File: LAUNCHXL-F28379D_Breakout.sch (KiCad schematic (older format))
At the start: 30 parts, among them Q1 100V/17A, Q2 100V/17A, Q3 100V/17A, Q4 100V/17A, Q5 100V/17A, Q6 100V/17A, U2 TL084CN, U5 STK681-332-E

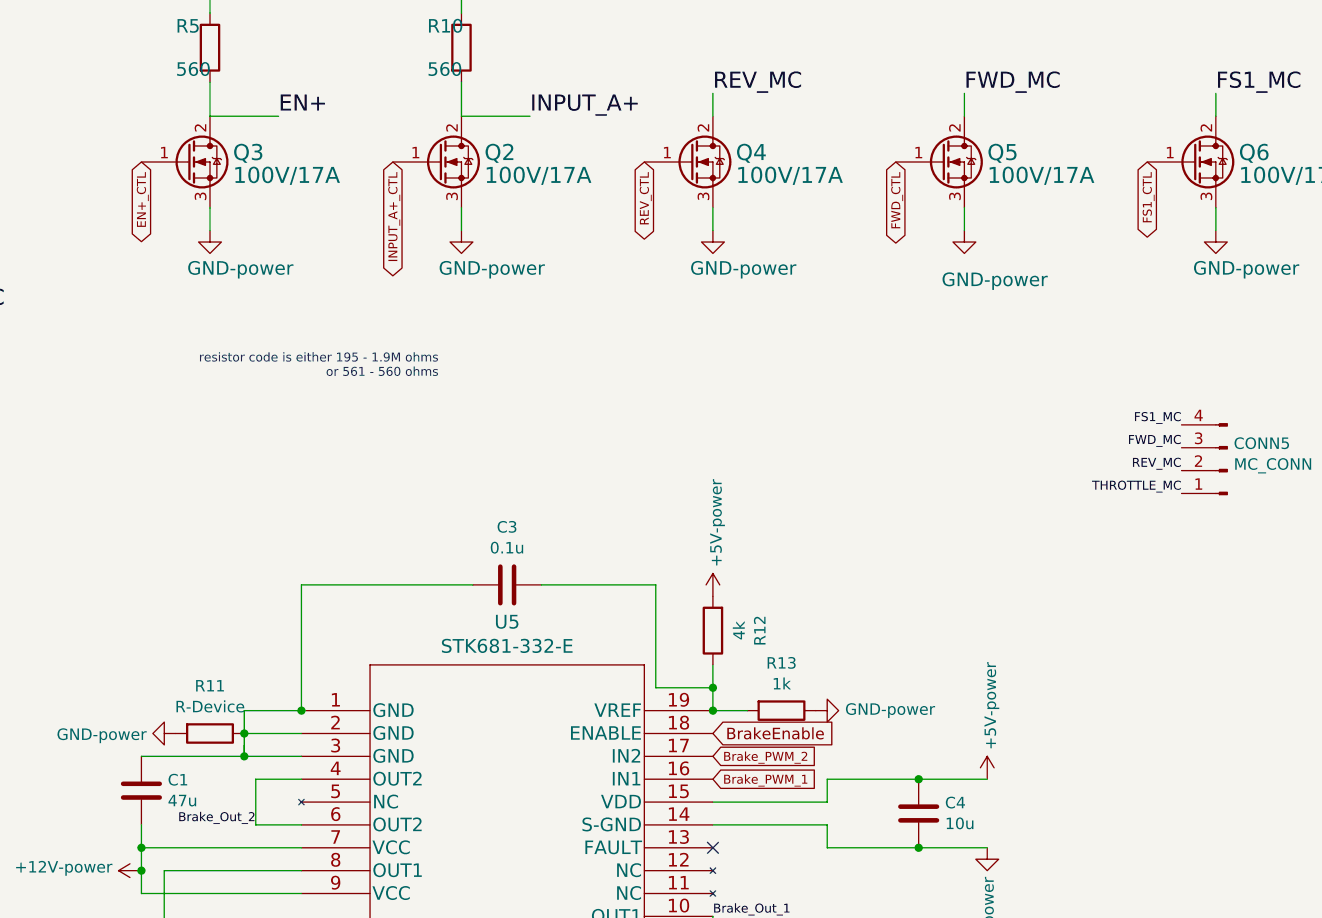
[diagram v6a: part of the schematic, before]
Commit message: updated PCB with bluetooth connector for arduino signals
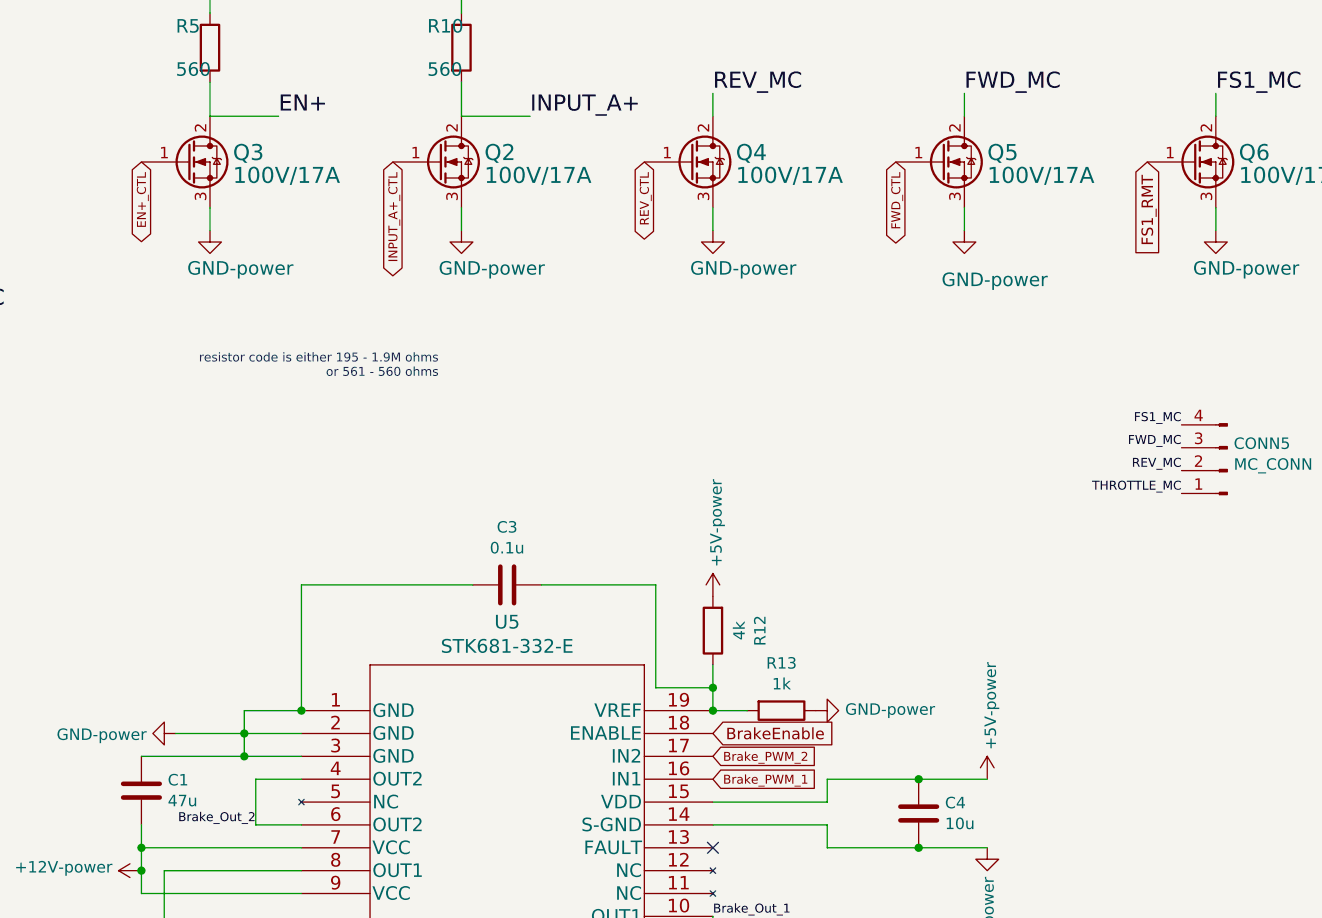
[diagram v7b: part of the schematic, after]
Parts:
- removed R11: R-Device, Resistor_THT:R_Axial_DIN0204_L3.6mm_D1.6mm_P1.90mm_Vertical, symbol PCB_2020-rescue:R-Device
- C1: footprint Capacitor_THT:C_Disc_D3.0mm_W1.6mm_P2.50mm -> Capacitor_THT:C_Radial_D4.0mm_H5.0mm_P1.50mm
- C3, C4: footprint Capacitor_THT:C_Disc_D3.0mm_W1.6mm_P2.50mm -> Capacitor_THT:CP_Radial_D4.0mm_P1.50mm
- R1, R12, R13, R18, R2, R3, R4, R5, R6, R7, R8, R9: footprint Resistor_THT:R_Axial_DIN0204_L3.6mm_D1.6mm_P1.90mm_Vertical -> Resistor_THT:R_Axial_DIN0204_L3.6mm_D1.6mm_P7.62mm_Horizontal
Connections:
- net GND: now also C1.2, C3.1, U5.1 (GND), U5.2 (GND), U5.3 (GND)
- net FS1_CTL renamed FS1_RMT
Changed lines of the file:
@@
 Text GLabel 9700 3200 3    39   BiDi ~ 0
 FWD_CTL
-Text GLabel 10800 3200 3    39   BiDi ~ 0
-FS1_CTL
 Text GLabel 7500 3200 3    39   BiDi ~ 0
 INPUT_A+_CTL
@@
 F 0 "R1" H 4600 1550 59  0000 L BNN
 F 1 "10k" H 4550 1450 59  0000 L BNN
-F 2 "Resistor_THT:R_Axial_DIN0204_L3.6mm_D1.6mm_P1.90mm_Vertical" H 4800 1500 50  0001 C CNN
+F 2 "Resistor_THT:R_Axial_DIN0204_L3.6mm_D1.6mm_P7.62mm_Horizontal" H 4800 1500 50  0001 C CNN
 F 3 "" H 4800 1500 50  0001 C CNN
 	1    4800 1500
@@
 F 0 "R5" H 6550 2759 59  0000 L BNN
 F 1 "560" H 6550 2570 59  0000 L BNN
-F 2 "Resistor_THT:R_Axial_DIN0204_L3.6mm_D1.6mm_P1.90mm_Vertical" H 6700 2700 50  0001 C CNN
+F 2 "Resistor_THT:R_Axial_DIN0204_L3.6mm_D1.6mm_P7.62mm_Horizontal" H 6700 2700 50  0001 C CNN
 F 3 "" H 6700 2700 50  0001 C CNN
 	1    6700 2700
@@
 F 0 "R10" H 7650 2759 59  0000 L BNN
 F 1 "560" H 7650 2570 59  0000 L BNN
-F 2 "Resistor_THT:R_Axial_DIN0204_L3.6mm_D1.6mm_P1.90mm_Vertical" H 7800 2700 50  0001 C CNN
+F 2 "Resistor_THT:R_Axial_DIN0204_L3.6mm_D1.6mm_P7.62mm_Horizontal" H 7800 2700 50  0001 C CNN
 F 3 "" H 7800 2700 50  0001 C CNN
 	1    7800 2700
@@
 F 0 "R2" H 5600 1500 59  0000 L BNN
 F 1 "10k" H 5550 1400 59  0000 L BNN
-F 2 "Resistor_THT:R_Axial_DIN0204_L3.6mm_D1.6mm_P1.90mm_Vertical" H 5800 1500 50  0001 C CNN
+F 2 "Resistor_THT:R_Axial_DIN0204_L3.6mm_D1.6mm_P7.62mm_Horizontal" H 5800 1500 50  0001 C CNN
 F 3 "" H 5800 1500 50  0001 C CNN
 	1    5800 1500
@@
 F 0 "R3" V 3143 3950 50  0000 C CNN
 F 1 "1000" V 3234 3950 50  0000 C CNN
-F 2 "Resistor_THT:R_Axial_DIN0204_L3.6mm_D1.6mm_P1.90mm_Vertical" V 3280 3950 50  0001 C CNN
+F 2 "Resistor_THT:R_Axial_DIN0204_L3.6mm_D1.6mm_P7.62mm_Horizontal" V 3280 3950 50  0001 C CNN
 F 3 "" H 3350 3950 50  0001 C CNN
 	1    3350 3950
@@
 F 0 "R7" V 4093 4750 50  0000 C CNN
 F 1 "5400" V 4184 4750 50  0000 C CNN
-F 2 "Resistor_THT:R_Axial_DIN0204_L3.6mm_D1.6mm_P1.90mm_Vertical" V 4230 4750 50  0001 C CNN
+F 2 "Resistor_THT:R_Axial_DIN0204_L3.6mm_D1.6mm_P7.62mm_Horizontal" V 4230 4750 50  0001 C CNN
 F 3 "" H 4300 4750 50  0001 C CNN
 	1    4300 4750
@@
 F 0 "R6" H 3420 3096 50  0000 L CNN
 F 1 "5400" H 3420 3005 50  0000 L CNN
-F 2 "Resistor_THT:R_Axial_DIN0204_L3.6mm_D1.6mm_P1.90mm_Vertical" V 3280 3050 50  0001 C CNN
+F 2 "Resistor_THT:R_Axial_DIN0204_L3.6mm_D1.6mm_P7.62mm_Horizontal" V 3280 3050 50  0001 C CNN
 F 3 "" H 3350 3050 50  0001 C CNN
 	1    3350 3050
@@
 F 0 "R4" V 2893 3400 50  0000 C CNN
 F 1 "1000" V 2984 3400 50  0000 C CNN
-F 2 "Resistor_THT:R_Axial_DIN0204_L3.6mm_D1.6mm_P1.90mm_Vertical" V 3030 3400 50  0001 C CNN
+F 2 "Resistor_THT:R_Axial_DIN0204_L3.6mm_D1.6mm_P7.62mm_Horizontal" V 3030 3400 50  0001 C CNN
 F 3 "" H 3100 3400 50  0001 C CNN
 	1    3100 3400
@@
 F 0 "R9" V 2743 4100 50  0000 C CNN
 F 1 "1000" V 2834 4100 50  0000 C CNN
-F 2 "Resistor_THT:R_Axial_DIN0204_L3.6mm_D1.6mm_P1.90mm_Vertical" V 2880 4100 50  0001 C CNN
+F 2 "Resistor_THT:R_Axial_DIN0204_L3.6mm_D1.6mm_P7.62mm_Horizontal" V 2880 4100 50  0001 C CNN
 F 3 "" H 2950 4100 50  0001 C CNN
 	1    2950 4100
@@
 F 0 "R8" V 2593 3950 50  0000 C CNN
 F 1 "5000" V 2684 3950 50  0000 C CNN
-F 2 "Resistor_THT:R_Axial_DIN0204_L3.6mm_D1.6mm_P1.90mm_Vertical" V 2730 3950 50  0001 C CNN
+F 2 "Resistor_THT:R_Axial_DIN0204_L3.6mm_D1.6mm_P7.62mm_Horizontal" V 2730 3950 50  0001 C CNN
 F 3 "" H 2800 3950 50  0001 C CNN
 	1    2800 3950
@@
 Connection ~ 6850 5700
 $Comp
-L PCB_2020-rescue:R-Device R11
-U 1 1 5FE58DCC
-P 6700 5700
-F 0 "R11" V 6493 5700 50  0000 C CNN
-F 1 "R-Device" V 6584 5700 50  0000 C CNN
-F 2 "Resistor_THT:R_Axial_DIN0204_L3.6mm_D1.6mm_P1.90mm_Vertical" V 6630 5700 50  0001 C CNN
-F 3 "" H 6700 5700 50  0001 C CNN
-	1    6700 5700
-	0    1    1    0
-$EndComp
-$Comp
 L PCB_2020-rescue:GND-power #PWR0111
 U 1 1 5FE59F80
@@
 F 0 "R13" V 8993 5600 50  0000 C CNN
 F 1 "1k" V 9084 5600 50  0000 C CNN
-F 2 "Resistor_THT:R_Axial_DIN0204_L3.6mm_D1.6mm_P1.90mm_Vertical" V 9130 5600 50  0001 C CNN
+F 2 "Resistor_THT:R_Axial_DIN0204_L3.6mm_D1.6mm_P7.62mm_Horizontal" V 9130 5600 50  0001 C CNN
 F 3 "" H 9200 5600 50  0001 C CNN
 	1    9200 5600
@@
 F 0 "R12" V 8693 5250 50  0000 C CNN
 F 1 "4k" V 8784 5250 50  0000 C CNN
-F 2 "Resistor_THT:R_Axial_DIN0204_L3.6mm_D1.6mm_P1.90mm_Vertical" V 8830 5250 50  0001 C CNN
+F 2 "Resistor_THT:R_Axial_DIN0204_L3.6mm_D1.6mm_P7.62mm_Horizontal" V 8830 5250 50  0001 C CNN
 F 3 "" H 8900 5250 50  0001 C CNN
 	1    8900 5250
@@
 F 0 "C4" H 9685 6004 50  0000 R CNN
 F 1 "10u" H 9685 6095 50  0000 R CNN
-F 2 "Capacitor_THT:C_Disc_D3.0mm_W1.6mm_P2.50mm" H 9838 5900 50  0001 C CNN
+F 2 "Capacitor_THT:CP_Radial_D4.0mm_P1.50mm" H 9838 5900 50  0001 C CNN
 F 3 "" H 9800 6050 50  0001 C CNN
 	1    9800 6050
@@
 F 0 "C1" H 6285 5904 50  0000 R CNN
 F 1 "47u" H 6285 5995 50  0000 R CNN
-F 2 "Capacitor_THT:C_Disc_D3.0mm_W1.6mm_P2.50mm" H 6438 5800 50  0001 C CNN
+F 2 "Capacitor_THT:C_Radial_D4.0mm_H5.0mm_P1.50mm" H 6438 5800 50  0001 C CNN
 F 3 "" H 6400 5950 50  0001 C CNN
 	1    6400 5950
@@
 F 0 "C3" V 8252 5050 50  0000 C CNN
 F 1 "0.1u" V 8161 5050 50  0000 C CNN
-F 2 "Capacitor_THT:C_Disc_D3.0mm_W1.6mm_P2.50mm" H 8038 4900 50  0001 C CNN
+F 2 "Capacitor_THT:CP_Radial_D4.0mm_P1.50mm" H 8038 4900 50  0001 C CNN
 F 3 "" H 8000 5050 50  0001 C CNN
 	1    8000 5050
@@
 	7100 5050 7100 5600
 Wire Wire Line
-	6850 5750 6850 5800
-Wire Wire Line
 	6850 5700 6850 5800
 Connection ~ 8900 5500
@@
 Wire Wire Line
 	7850 5050 7100 5050
+Wire Wire Line
+	6850 5700 6550 5700
+Text GLabel 10800 3200 3    50   Input ~ 0
+FS1_RMT
 $EndSCHEMATC

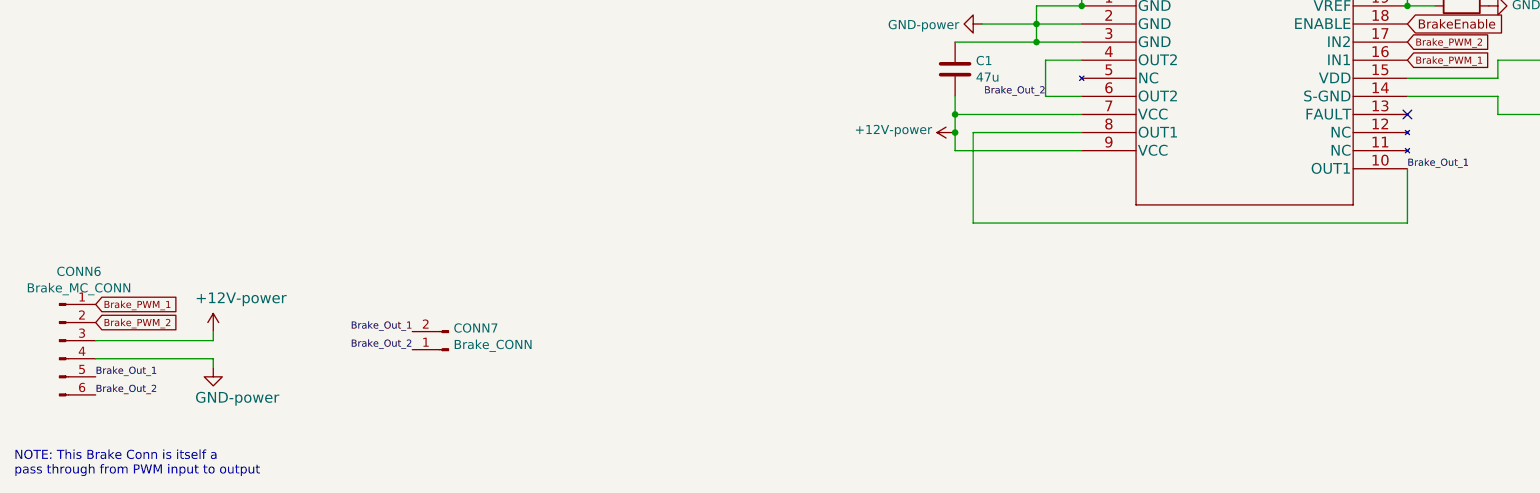
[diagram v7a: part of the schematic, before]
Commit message: updated trace width
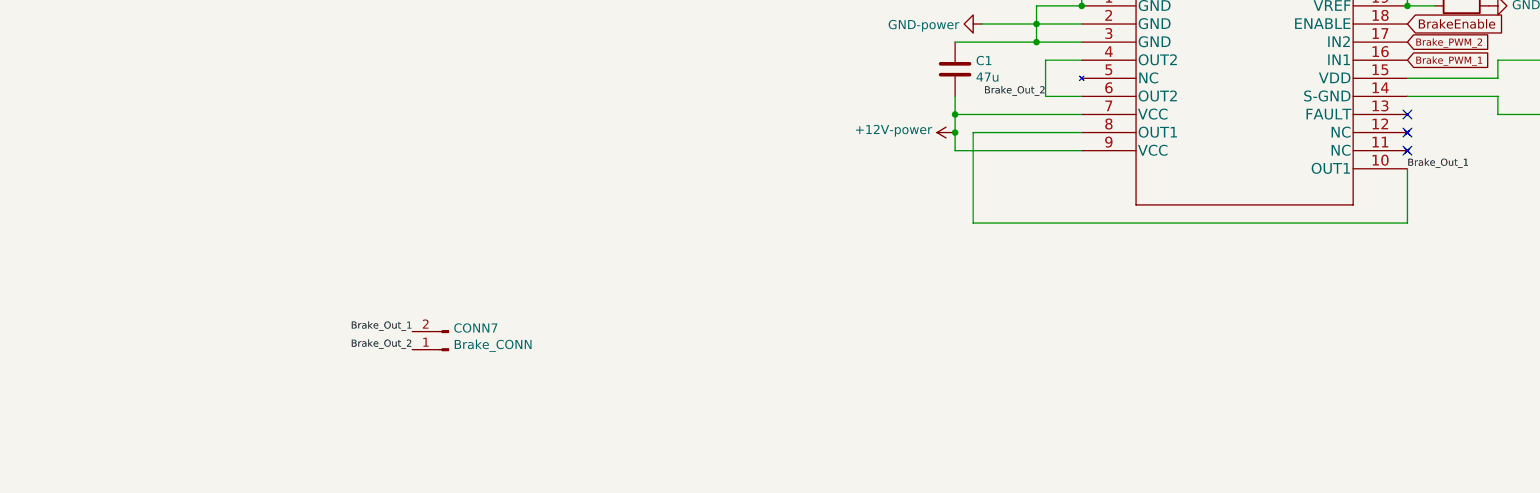
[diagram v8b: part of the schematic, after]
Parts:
- removed CONN6: Brake_MC_CONN, Drivetrain_control:Brake_MC_Conn_6_pin, symbol PCB_2020-rescue:Conn_01x06_Male-Connector
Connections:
- no-connect marks 1 -> 3
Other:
- note removed: "NOTE: This Brake Conn is itself a\npass through from PWM input to output\n"
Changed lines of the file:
@@
 	1    0    0    -1
 $EndComp
-Text GLabel 1650 7350 2    39   Input ~ 0
-Brake_PWM_2
-Text GLabel 1650 7250 2    39   Input ~ 0
-Brake_PWM_1
-$Comp
-L PCB_2020-rescue:GND-power #GND?
-U 1 1 5E188E1D
-P 2300 7600
-AR Path="/5E188E1D" Ref="#GND?"  Part="1"
-AR Path="/5DD5E236/5E188E1D" Ref="#GND?"  Part="1"
-AR Path="/5DF27AC1/5E188E1D" Ref="#GND0101"  Part="1"
-F 0 "#GND0101" H 2300 7600 50  0001 C CNN
-F 1 "GND-power" H 2200 7400 59  0000 L BNN
-F 2 "" H 2300 7600 50  0001 C CNN
-F 3 "" H 2300 7600 50  0001 C CNN
-	1    2300 7600
-	1    0    0    -1
-$EndComp
-$Comp
-L PCB_2020-rescue:+12V-power #P+?
-U 1 1 5E189D98
-P 2300 7400
-AR Path="/5E189D98" Ref="#P+?"  Part="1"
-AR Path="/5DD5E236/5E189D98" Ref="#P+?"  Part="1"
-AR Path="/5DF27AC1/5E189D98" Ref="#P+0101"  Part="1"
-F 0 "#P+0101" H 2300 7400 50  0001 C CNN
-F 1 "+12V-power" H 2200 7550 59  0000 L BNN
-F 2 "" H 2300 7400 50  0001 C CNN
-F 3 "" H 2300 7400 50  0001 C CNN
-	1    2300 7400
-	1    0    0    -1
-$EndComp
-Wire Wire Line
-	1650 7450 2300 7450
-Wire Wire Line
-	2300 7450 2300 7400
-Wire Wire Line
-	1650 7550 2300 7550
-Wire Wire Line
-	2300 7550 2300 7600
 $Comp
 L PCB_2020-rescue:Conn_01x02_Male-Connector CONN7
@@
 Text Label 3400 7400 2    39   ~ 0
 Brake_Out_1
-Text Label 1650 7650 0    39   ~ 0
-Brake_Out_1
 Text Label 3400 7500 2    39   ~ 0
 Brake_Out_2
-Text Label 1650 7750 0    39   ~ 0
-Brake_Out_2
-Text Notes 1200 8200 0    50   ~ 0
-NOTE: This Brake Conn is itself a\npass through from PWM input to output\n
 $Comp
 L PCB_2020-rescue:Q_NMOS_GDS-Device Q?
@@
 	2150 3950 2650 3950
 $Comp
-L PCB_2020-rescue:Conn_01x06_Male-Connector CONN6
-U 1 1 5E187579
-P 1450 7450
-F 0 "CONN6" H 1558 7831 50  0000 C CNN
-F 1 "Brake_MC_CONN" H 1558 7740 50  0000 C CNN
-F 2 "Drivetrain_control:Brake_MC_Conn_6_pin" H 1450 7450 50  0001 C CNN
-F 3 "https://cdn-shop.adafruit.com/product-files/3190/drv8871.pdf" H 1450 7450 50  0001 C CNN
-F 4 "https://learn.adafruit.com/adafruit-drv8871-brushed-dc-motor-driver-breakout/" H 1450 7450 50  0001 C CNN "Website"
-	1    1450 7450
-	1    0    0    -1
-$EndComp
-$Comp
 L 2020-12-20_21-08-33:STK681-332-E U5
 U 1 1 5FE14AEF
@@
 Text GLabel 10800 3200 3    50   Input ~ 0
 FS1_RMT
+NoConn ~ 8900 6300
+NoConn ~ 8900 6400
 $EndSCHEMATC
